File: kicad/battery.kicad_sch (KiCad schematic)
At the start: 14 parts

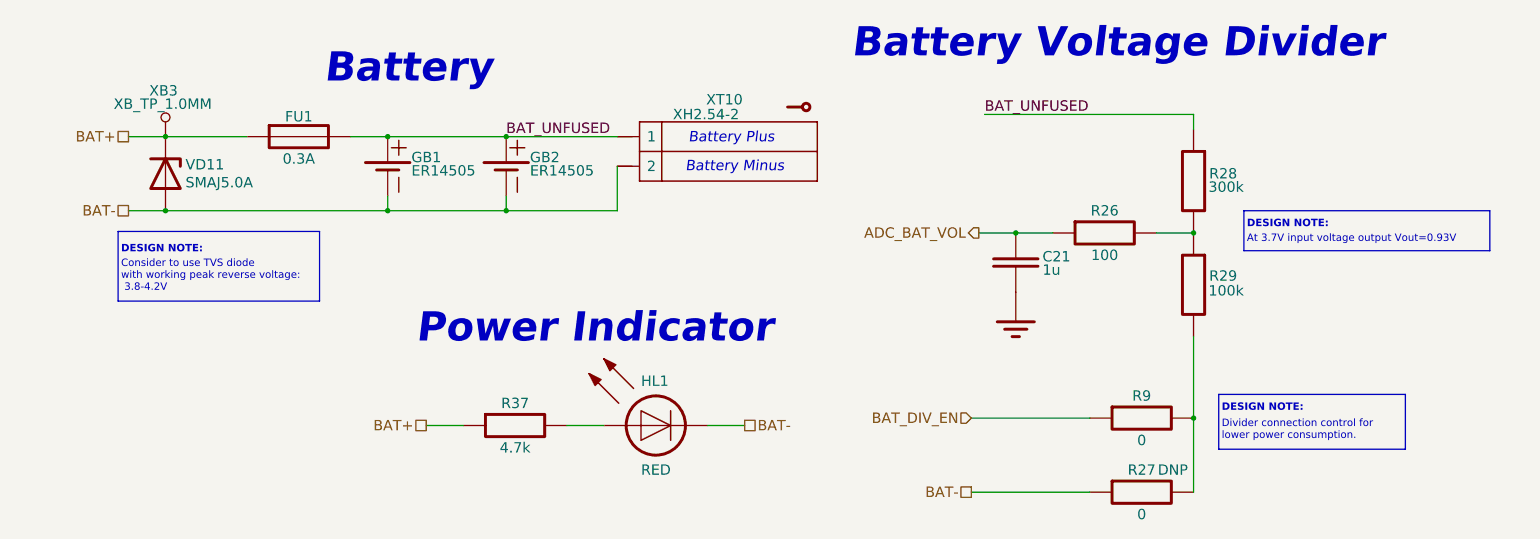
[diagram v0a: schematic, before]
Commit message: Reannotate schematic; Fix 5032 crystal footprint field; Update PCB with 5032 crystal
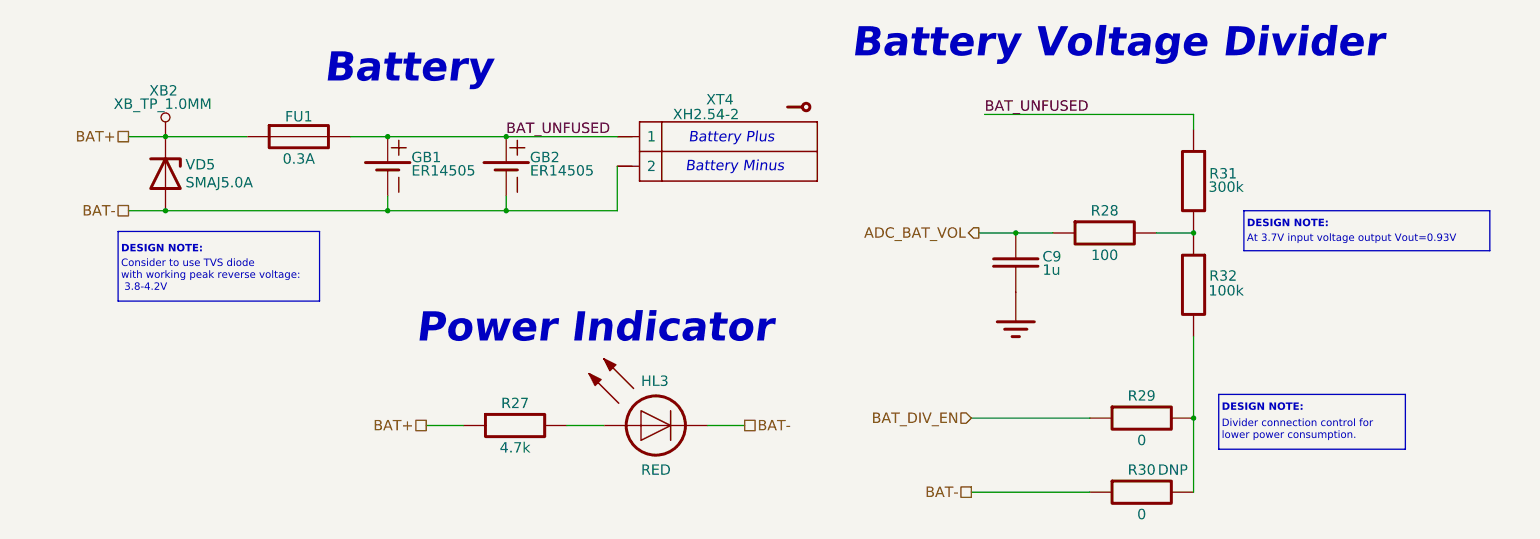
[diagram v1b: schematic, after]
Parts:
- renumbered C21 to C9, HL1 to HL3, R37 to R27, R26 to R28, R9 to R29, R27 to R30, R28 to R31, R29 to R32, VD11 to VD5, XB3 to XB2, XT10 to XT4
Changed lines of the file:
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@@
   (symbol (lib_id "Resistors:R_RES") (at 227.838 98.806 270) (unit 1)
     (in_bom yes) (on_board yes)
-    (property "Reference" "R29" (id 0) (at 232.918 97.282 90)
+    (property "Reference" "R32" (id 0) (at 232.918 97.282 90)
       (effects (font (size 1.778 1.778)))
     )
@@
   (symbol (lib_id "Resistors:R_RES") (at 111.506 122.936 0) (unit 1)
     (in_bom yes) (on_board yes)
-    (property "Reference" "R37" (id 0) (at 111.506 119.126 0)
+    (property "Reference" "R27" (id 0) (at 111.506 119.126 0)
       (effects (font (size 1.778 1.778)))
     )
@@
   (symbol (lib_id "Resistors:R_RES") (at 212.598 89.916 0) (unit 1)
     (in_bom yes) (on_board yes)
-    (property "Reference" "R26" (id 0) (at 212.598 86.106 0)
+    (property "Reference" "R28" (id 0) (at 212.598 86.106 0)
       (effects (font (size 1.778 1.778)))
     )
@@
   (symbol (lib_id "Resistors:R_RES") (at 218.948 134.366 0) (unit 1)
     (in_bom yes) (on_board yes)
-    (property "Reference" "R27" (id 0) (at 218.948 130.556 0)
+    (property "Reference" "R30" (id 0) (at 218.948 130.556 0)
       (effects (font (size 1.778 1.778)))
     )
@@
   (symbol (lib_id "Diodes:HL_LED") (at 135.636 122.936 0) (unit 1)
     (in_bom yes) (on_board yes)
-    (property "Reference" "HL1" (id 0) (at 133.096 115.316 0)
+    (property "Reference" "HL3" (id 0) (at 133.096 115.316 0)
       (effects (font (size 1.778 1.778)) (justify left))
     )
@@
   (symbol (lib_id "Diodes:D_ZENER_SPICE") (at 51.562 79.756 90) (unit 1)
     (in_bom yes) (on_board yes)
-    (property "Reference" "VD11" (id 0) (at 54.991 78.2066 90)
+    (property "Reference" "VD5" (id 0) (at 54.991 78.2066 90)
       (effects (font (size 1.778 1.778)) (justify right))
     )
@@
   (symbol (lib_id "Connectors:XB_TP_1.0MM") (at 51.562 73.406 0) (unit 1)
     (in_bom no) (on_board yes)
-    (property "Reference" "XB3" (id 0) (at 48.768 65.532 0)
+    (property "Reference" "XB2" (id 0) (at 48.768 65.532 0)
       (effects (font (size 1.778 1.778)) (justify left))
     )
@@
   (symbol (lib_id "Capacitors:C_CAP") (at 197.358 94.996 270) (unit 1)
     (in_bom yes) (on_board yes)
-    (property "Reference" "C21" (id 0) (at 201.93 93.98 90)
+    (property "Reference" "C9" (id 0) (at 201.93 93.98 90)
       (effects (font (size 1.778 1.778)) (justify left))
     )
@@
   (symbol (lib_id "Resistors:R_RES") (at 227.838 81.026 270) (unit 1)
     (in_bom yes) (on_board yes)
-    (property "Reference" "R28" (id 0) (at 232.918 79.756 90)
+    (property "Reference" "R31" (id 0) (at 232.918 79.756 90)
       (effects (font (size 1.778 1.778)))
     )
@@
   (symbol (lib_id "Power:GROUND") (at 197.358 105.156 0) (unit 1)
     (in_bom yes) (on_board yes)
-    (property "Reference" "#PWR038" (id 0) (at 197.358 110.236 0)
+    (property "Reference" "#PWR030" (id 0) (at 197.358 110.236 0)
       (effects (font (size 1.778 1.778)) hide)
     )
@@
   (symbol (lib_id "Resistors:R_RES") (at 218.948 121.666 0) (unit 1)
     (in_bom yes) (on_board yes)
-    (property "Reference" "R9" (id 0) (at 218.948 117.856 0)
+    (property "Reference" "R29" (id 0) (at 218.948 117.856 0)
       (effects (font (size 1.778 1.778)))
     )
@@
   (symbol (lib_id "Connectors:XT_CONTACT_ARR2") (at 146.812 75.946 0) (unit 1)
     (in_bom yes) (on_board yes)
-    (property "Reference" "XT10" (id 0) (at 144.272 67.056 0)
-      (effects (font (size 1.778 1.778)) (justify left))
-    )
+    (property "Reference" "XT4" (id 0) (at 144.272 67.056 0)
+      (effects (font (size 1.778 1.778)) (justify left))
+    )

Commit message: Add voltage value to caps, update BOM, SCH, ASM
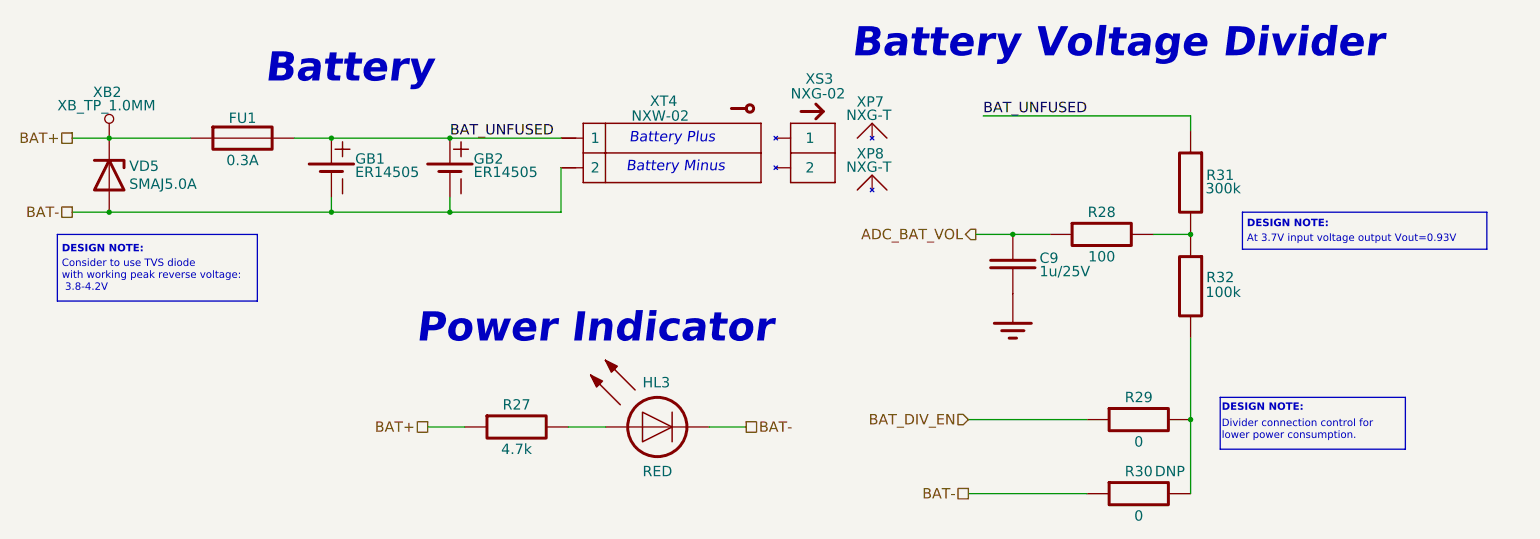
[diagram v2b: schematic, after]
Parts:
- added XP7, XP8: NXG-T, symbol Connectors:XS_TERMINAL
- added XS3: NXG-02, symbol Connectors:XS_PLUG2
- C9: value 1u -> 1u/25V; Case/Package (none) -> 0603; Tolerance (none) -> ±10%; Type (none) -> X7R
- R27, R28, R29, R30, R31, R32: Case/Package 0000 -> 0603; Tolerance ±% -> ±5%
- XT4: value XH2.54-2 -> NXW-02
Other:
- moved on the sheet: C9, FU1, GB1, GB2, R28, R29, R30, R31, R32, VD5, XB2, XT4

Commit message: Add wiring diagram; Add work ours (stage 2); refactor folders
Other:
- title: (none) -> RadioSens v1
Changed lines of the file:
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@@
 (kicad_sch (version 20211123) (generator eeschema)
   (paper "A4")
+  (title_block
+    (title "RadioSens v1")
+    (comment 2 "Electrical Circuit")
+  )
   (junction (at 80.01 86.36) (diameter 0) (color 0 0 0 0)
   )
